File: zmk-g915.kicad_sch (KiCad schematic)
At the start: 53 parts, among them J1 Prog_conn, J2 Tag connect TC2030-CTX, J3 53047-0460, Q3 Q_NMOS, SW1 Reset Switch, U1 nRF52840-QIAA-R/nRF52833-QIAA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, U2 SN74AHCT1G125, Y1 32.768kHz, Y2 32MHz

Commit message: led matrix sheet
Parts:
- removed R18: 10k, Resistor_SMD:R_0402_1005Metric, symbol keyboard:R_US
- removed R8: 100, Resistor_SMD:R_0402_1005Metric, symbol keyboard:R_US
- removed U2: SN74AHCT1G125, Package_TO_SOT_SMD:SOT-23-5, symbol keyboard:74LVC1G125
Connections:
- net MCU_RGB is gone; now on net CAPS_LED: U1.B13 (P0.03/AIN1)
- net ~{RGB_EN} is gone; now on net LBAT_LED: U1.K2 (P0.05/AIN3)
- net CAPS_LED: no longer U1.B19 (P1.11)
- net LBAT_LED: no longer U1.P2 (P1.08)
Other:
- added sheet rgb-led_matrix (rgb-led_matrix.kicad_sch)
- company: HW-tinkerers -> (none)
- title: Main Page -> (none)

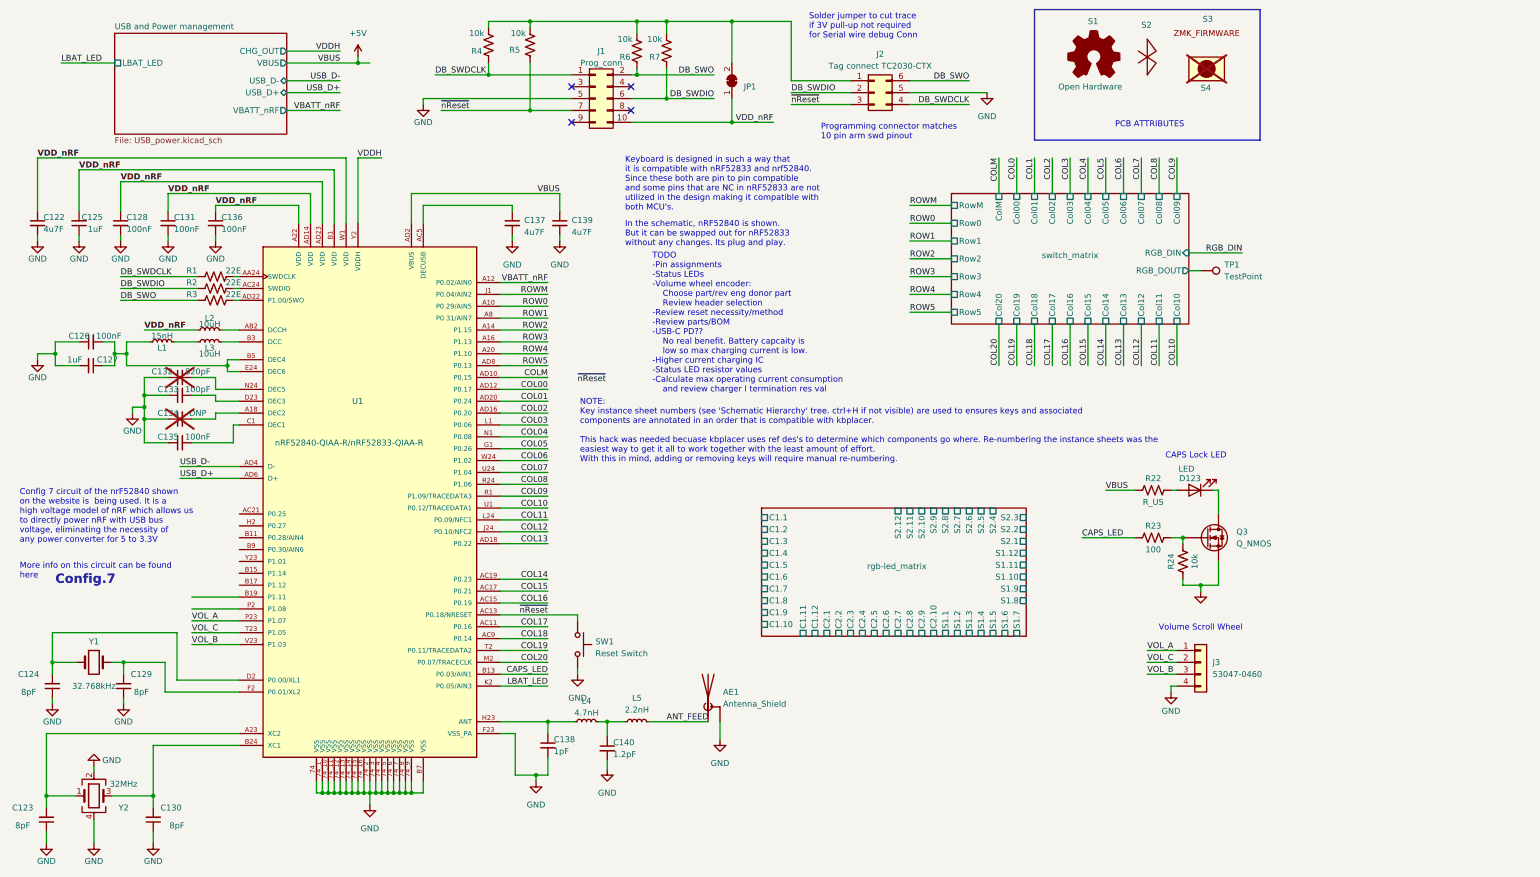
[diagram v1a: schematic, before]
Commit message: g915 and k618 pcb key and cutout placement
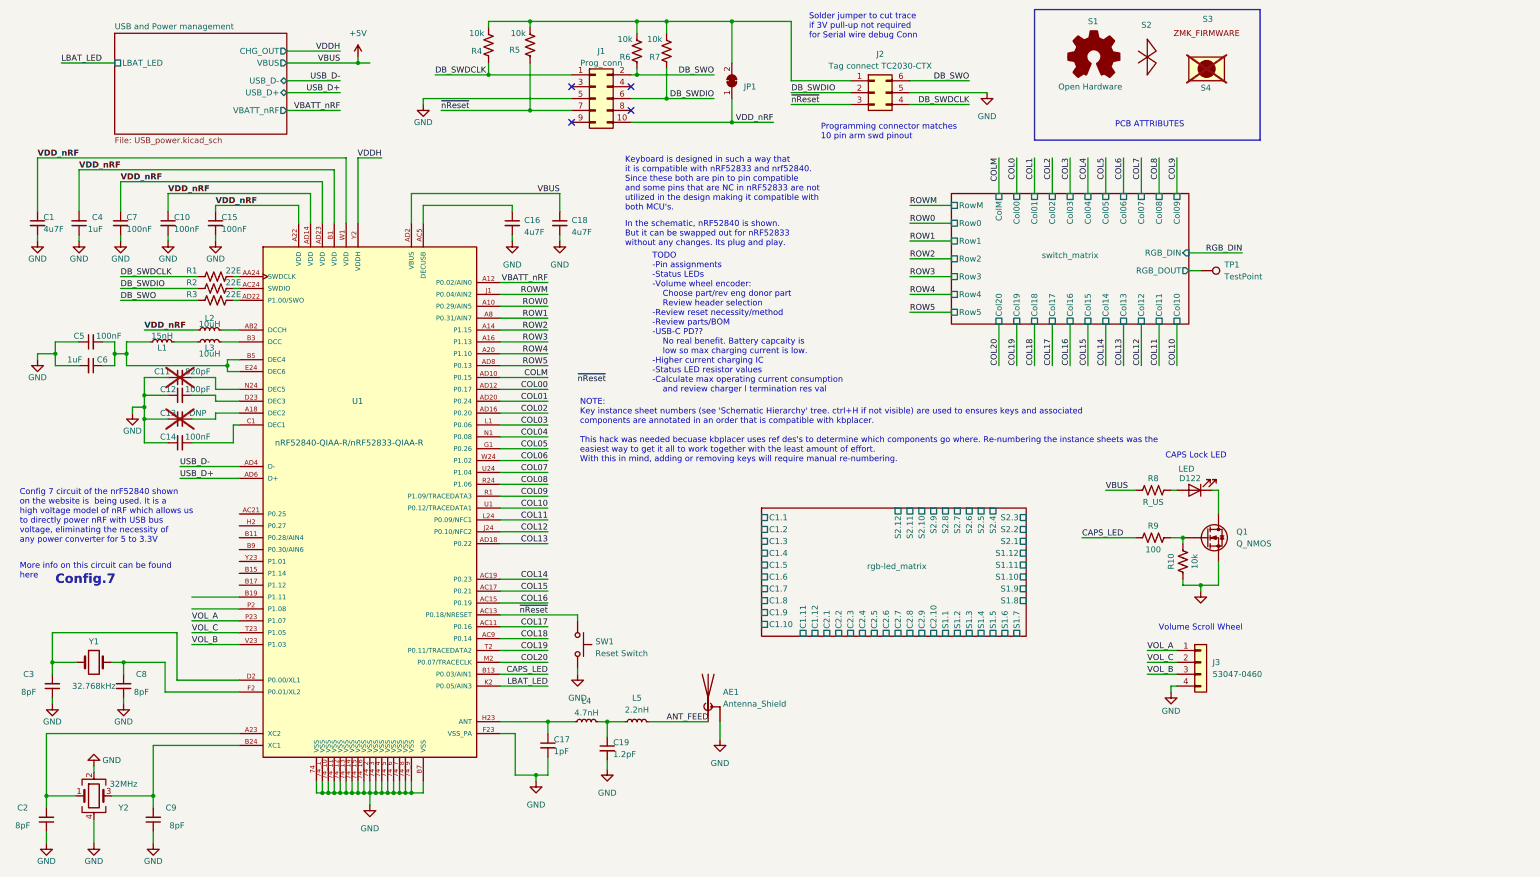
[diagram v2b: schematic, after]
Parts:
- S4: footprint keyboard:Keybaord_outline_edgecuts -> (none)
- renumbered C122 to C1, C131 to C10, C132 to C11, C133 to C12, C134 to C13, C135 to C14, C136 to C15, C137 to C16, C138 to C17, C139 to C18, C140 to C19, C123 to C2, C124 to C3, C125 to C4, C126 to C5, C127 to C6, C128 to C7, C129 to C8, C130 to C9, D123 to D122, Q3 to Q1, R24 to R10, R22 to R8, R23 to R9

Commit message: Minor pcb layout changes. Add matrix led drivers
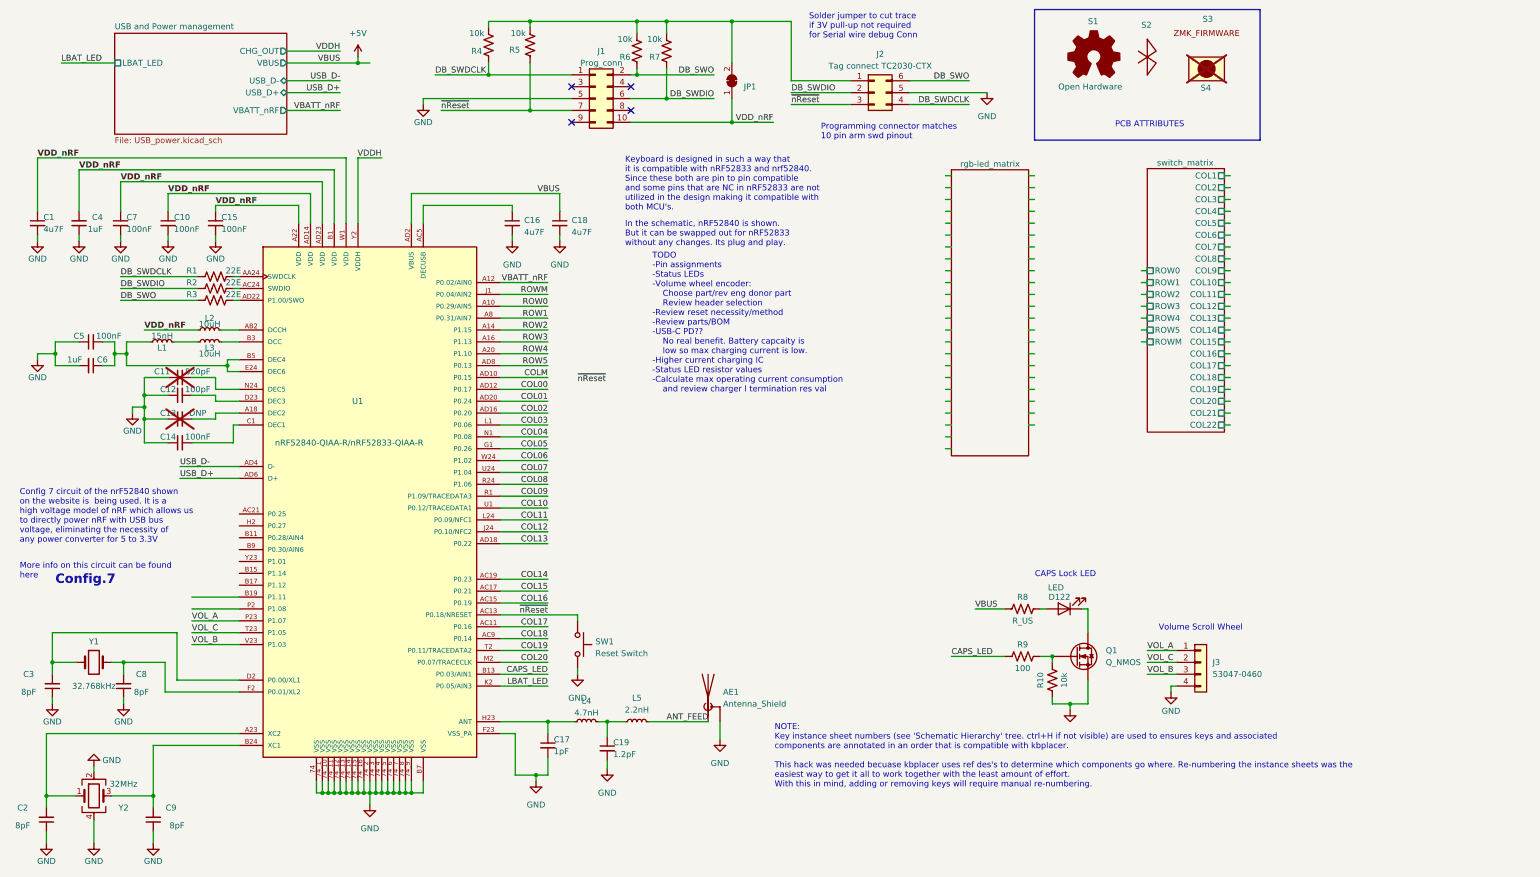
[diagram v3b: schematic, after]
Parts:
- removed TP1: TestPoint, TestPoint:TestPoint_Pad_D1.5mm, symbol Connector:TestPoint
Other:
- sheet rgb-led_matrix ports: added none; removed C1.1, C1.10, C1.11, C1.12, C1.2, C1.3, C1.4, C1.5, C1.6, C1.7, C1.8, C1.9, C2.1, C2.10, C2.2, C2.3, C2.4, C2.5, C2.6, C2.7, C2.8, C2.9, S1.1, S1.10, S1.11, S1.12, S1.2, S1.3, S1.4, S1.5, S1.6, S1.7, S1.8, S1.9, S2.1, S2.10, S2.11, S2.12, S2.2, S2.3, S2.4, S2.5, S2.6, S2.7, S2.8, S2.9
- sheet switch_matrix ports: added COL1, COL10, COL11, COL12, COL13, COL14, COL15, COL16, COL17, COL18, COL19, COL2, COL20, COL21, COL22, COL3, COL4, COL5, COL6, COL7, COL8, COL9, ROW0, ROW1, ROW2, ROW3, ROW4, ROW5, ROWM; removed Col00, Col01, Col02, Col03, Col04, Col05, Col06, Col07, Col08, Col09, Col10, Col11, Col12, Col13, Col14, Col15, Col16, Col17, Col18, Col19, Col20, ColM, RGB_DIN, RGB_DOUT, Row0, Row1, Row2, Row3, Row4, Row5, RowM
- moved on the sheet: D122, Q1, R10, R8, R9

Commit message: led matrix work
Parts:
- C1, C16, C18: value 4u7F -> 4.7uF
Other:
- note added: "TODO -Pin assignments -Status LEDs -Volume wheel encoder: Choose part/rev eng donor part Review header selection -Review reset necessity/method -Review parts/BOM -USB-C PD?? No real benefit. Battery capcaity is low so max charging current is low. -Higher current charging IC -Status LED resistor values -Calculate max operating current consumption and review charger I termination res val -Choose be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"
- note removed: "TODO -Pin assignments -Status LEDs -Volume wheel encoder: Choose part/rev eng donor part Review header selection -Review reset necessity/method -Review parts/BOM -USB-C PD?? No real benefit. Battery capcaity is low so max charging current is low. -Higher current charging IC -Status LED resistor values -Calculate max operating current consumption and review charger I termination res val"
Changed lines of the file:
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@@
 		)
 	)
-	(text "TODO\n-Pin assignments\n-Status LEDs\n-Volume wheel encoder:\n	Choose part/rev eng donor part\n	Review header selection\n-Review reset necessity/method\n-Review parts/BOM\n-USB-C PD??\n	No real benefit. Battery capcaity is\n	low so max charging current is low.\n-Higher current charging IC\n-Status LED resistor values\n-Calculate max operating current consumption\n	and review charger I termination res val"
+	(text "TODO\n-Pin assignments\n-Status LEDs\n-Volume wheel encoder:\n	Choose part/rev eng donor part\n	Review header selection\n-Review reset necessity/method\n-Review parts/BOM\n-USB-C PD??\n	No real benefit. Battery capcaity is\n	low so max charging current is low.\n-Higher current charging IC\n-Status LED resistor values\n-Calculate max operating current consumption\n	and review charger I termination res val\n-Choose between nRF52840 and nRF52833"
 		(exclude_from_sim no)
-		(at 151.892 81.026 0)
+		(at 148.59 84.074 0)
 		(effects
 			(font
@@
 			)
 		)
-		(property "Value" "4u7F"
+		(property "Value" "4.7uF"
 			(at 21.59 60.96 0)
 			(effects
@@
 		(fields_autoplaced yes)
 		(property "Reference" "C16"
-			(at 124.46 59.0613 0)
+			(at 124.46 58.4262 0)
 			(effects
 				(font
@@
 			)
 		)
-		(property "Value" "4u7F"
-			(at 124.46 61.6013 0)
+		(property "Value" "4.7uF"
+			(at 124.46 60.9662 0)
 			(effects
 				(font
@@
 		(fields_autoplaced yes)
 		(property "Reference" "C18"
-			(at 134.62 59.0613 0)
+			(at 134.62 58.4262 0)
 			(effects
 				(font
@@
 			)
 		)
-		(property "Value" "4u7F"
-			(at 134.62 61.6013 0)
+		(property "Value" "4.7uF"
+			(at 134.62 60.9662 0)
 			(effects
 				(font
@@
 			)
 		)
-		(pin "USB_D-" bidirectional
+		(pin "USB_D-" passive
 			(at 73.66 29.21 0)
 			(effects
@@
 			)
 		)
-		(pin "VBATT_nRF" output
+		(pin "VBATT_nRF" passive
 			(at 73.66 35.56 0)
 			(effects
@@
 			)
 		)
-		(pin "USB_D+" bidirectional
+		(pin "USB_D+" passive
 			(at 73.66 31.75 0)
 			(effects
@@
 			)
 		)
-		(pin "VBUS" output
+		(pin "VBUS" passive
 			(at 73.66 25.4 0)
 			(effects
@@
 			)
 		)
-		(pin "CHG_OUT" output
+		(pin "CHG_OUT" passive
 			(at 73.66 22.86 0)
 			(effects
